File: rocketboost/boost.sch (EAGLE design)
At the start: 15 parts, among them J1 RASPBERRYPI-40-PIN-GPIO_PTH_N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, U1 TPS61232DRCR

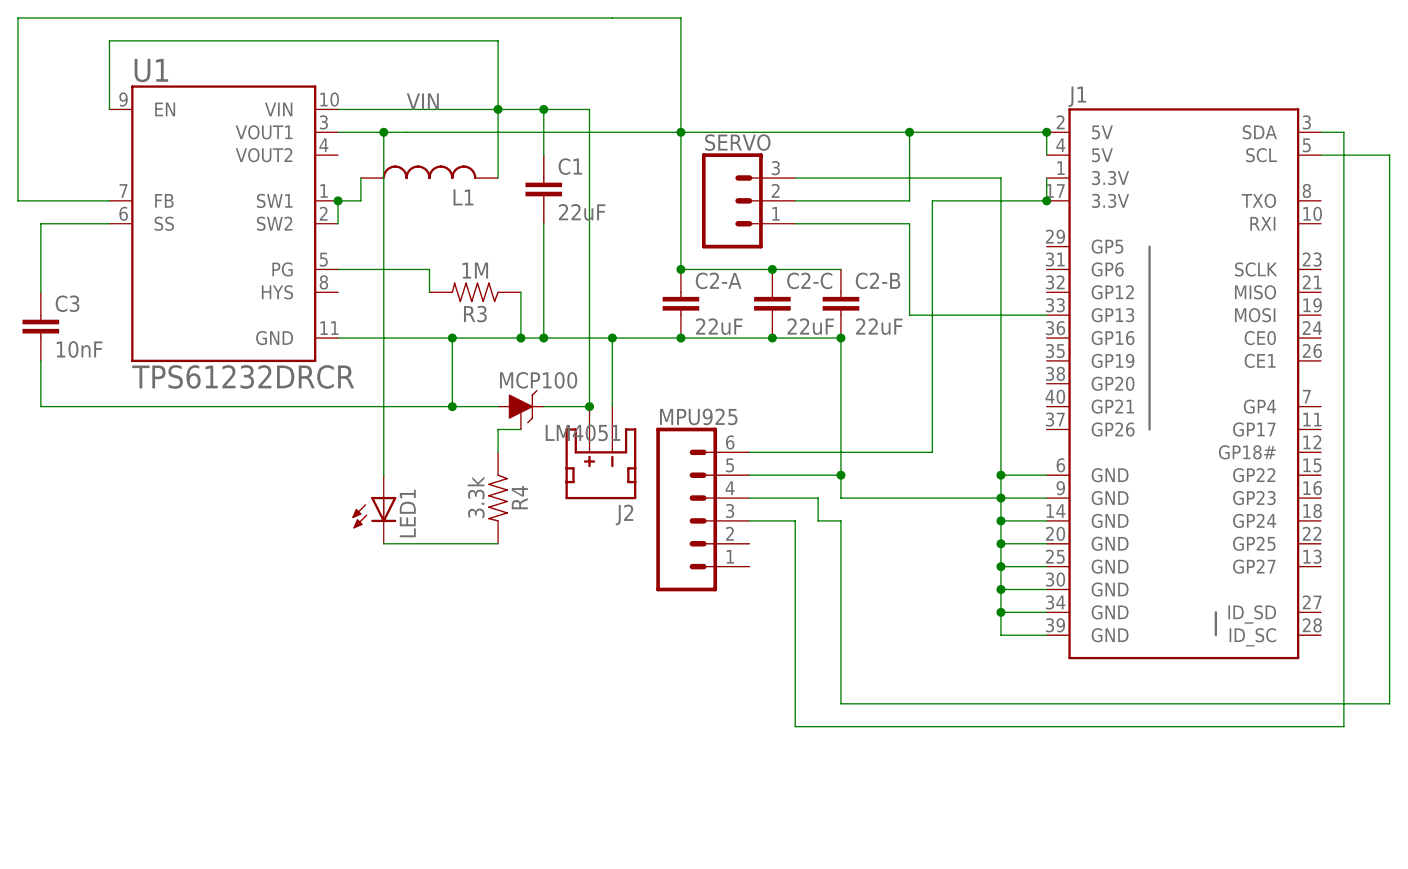
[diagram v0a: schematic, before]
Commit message: board with ground proper to 61232
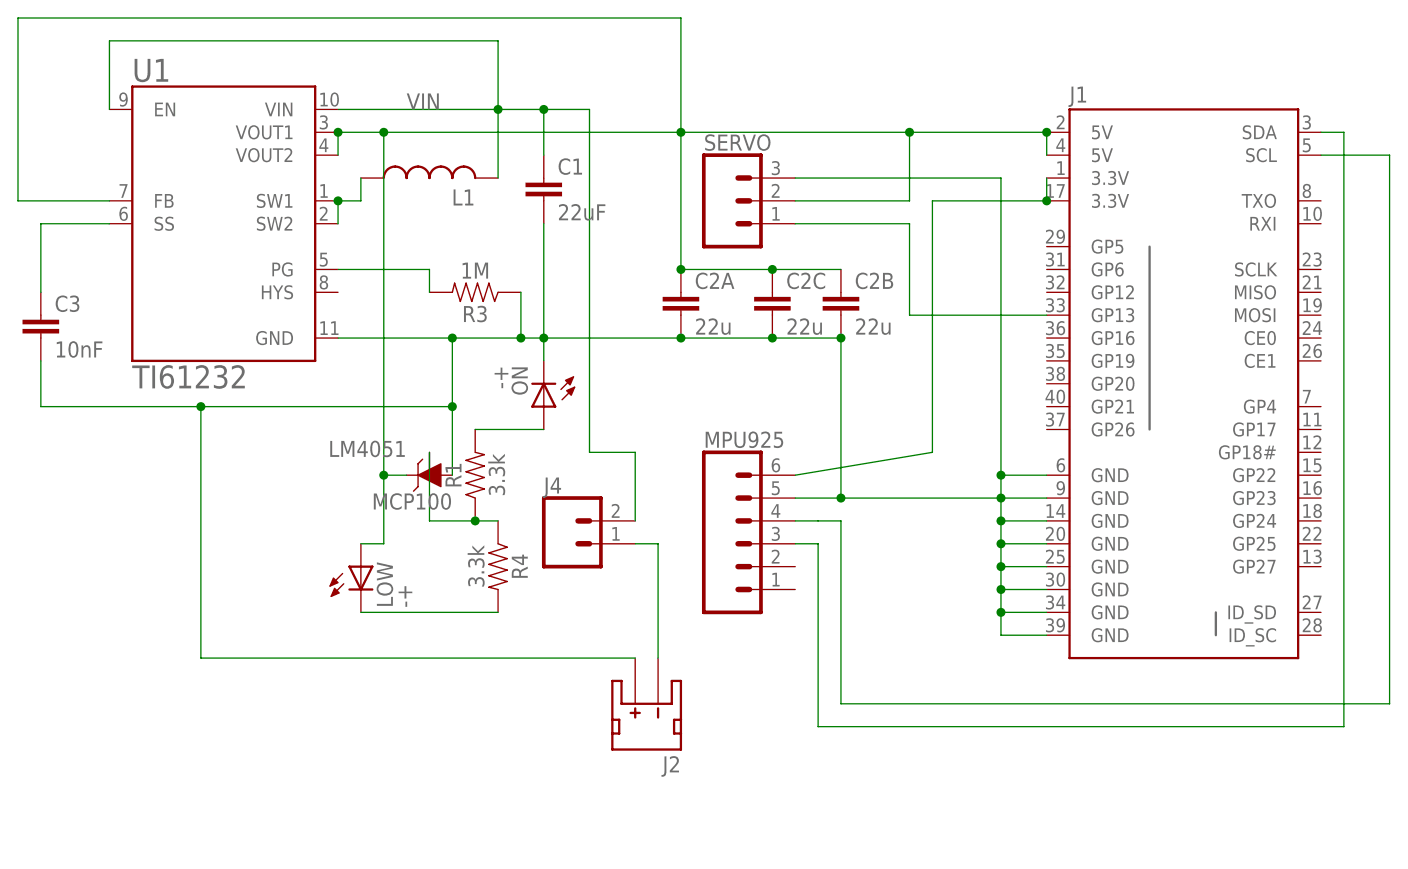
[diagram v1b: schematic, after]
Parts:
- removed LED1: (no value), led:LEDCHIP-LED0603
- added J4: (no value), SparkFun-Connectors:CONN_02LOCK
- added LOW, ON: -+, led:LEDCHIP-LED0603
- added R1: 3.3k, SparkFun-Resistors:3.3KOHM-0603-1/10W-1%
- C2A, C2B, C2C: value 22uF -> 22u
- U1: value TPS61232DRCR -> TI61232; device TPS61232DRCR:TPS61232DRCR -> TPS61232DRCR-1:TI61232
- renumbered C2-A to C2A, C2-B to C2B, C2-C to C2C
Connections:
- net N$9 renamed PWM
- new net N$1: J2.-, J4.1
- new net N$2: ON.A, R1.2
- net GND: now also J2.+, ON.C; no longer J2.-
- net N$13: now also LOW.C; no longer LED1.C
- net N$4: now also R1.1
- net VIN: now also J4.2; no longer J2.+, MCP100.C
- net VOUT: now also LOW.A, MCP100.C, U1.VOUT2; no longer LED1.A
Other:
- moved on the sheet: J2, MCP100, MPU925, R4

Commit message: ver 2.0
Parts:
- removed J4: (no value), SparkFun-Connectors:CONN_02LOCK
- removed LOW, ON: -+, led:LEDCHIP-LED0603
- removed MPU925: (no value), SparkFun-Connectors:CONN_06POLAR
- added 3.3-GND-SCL-SDA: (no value), SparkFun-Connectors:CONN_06POLAR
- added J3: SWITCH, SparkFun-Connectors:CONN_02
- added LED1: LO, led:LEDCHIP-LED0603
- added LED2: ok, led:LEDCHIP-LED0603
- C2-A, C2-B, C2-C: value 22u -> 22uF
- J2: value (none) -> PWR
- U1: value TI61232 -> TPS61232DRCR; device TPS61232DRCR-1:TI61232 -> steveo:TPS61232DRCR
- renumbered C2A to C2-A, C2B to C2-B, C2C to C2-C, SERVO to GND-5.0-PWM
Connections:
- net PWM renamed N$9
- removed net N$2: ON.A, R1.2
- new net N$22: J2.-, J3.2
- net GND: now also 3.3-GND-SCL-SDA.5, R1.1; no longer MPU925.5, ON.C
- net N$1: now also LED2.C, R1.2; no longer J2.-, J4.1
- net N$13: now also LED1.C; no longer LOW.C
- net N$4: now also LED2.A; no longer R1.1
- net SCL: now also 3.3-GND-SCL-SDA.4; no longer MPU925.4
- net SDA: now also 3.3-GND-SCL-SDA.3; no longer MPU925.3
- net V33: now also 3.3-GND-SCL-SDA.6; no longer MPU925.6
- net VIN: now also J3.1; no longer J4.2
- net VOUT: now also LED1.A; no longer LOW.A
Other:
- moved on the sheet: J2, L1, MCP100, R1, R4
